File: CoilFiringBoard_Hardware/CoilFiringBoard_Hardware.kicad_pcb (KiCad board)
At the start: 2 copper layers, 96.5 x 71.1 mm, 19 parts, among them Q1 Q_NMOS_GDS, Q2 Q_NMOS_GDS, Q3 Q_NMOS_GDS, Q4 Q_NMOS_GDS

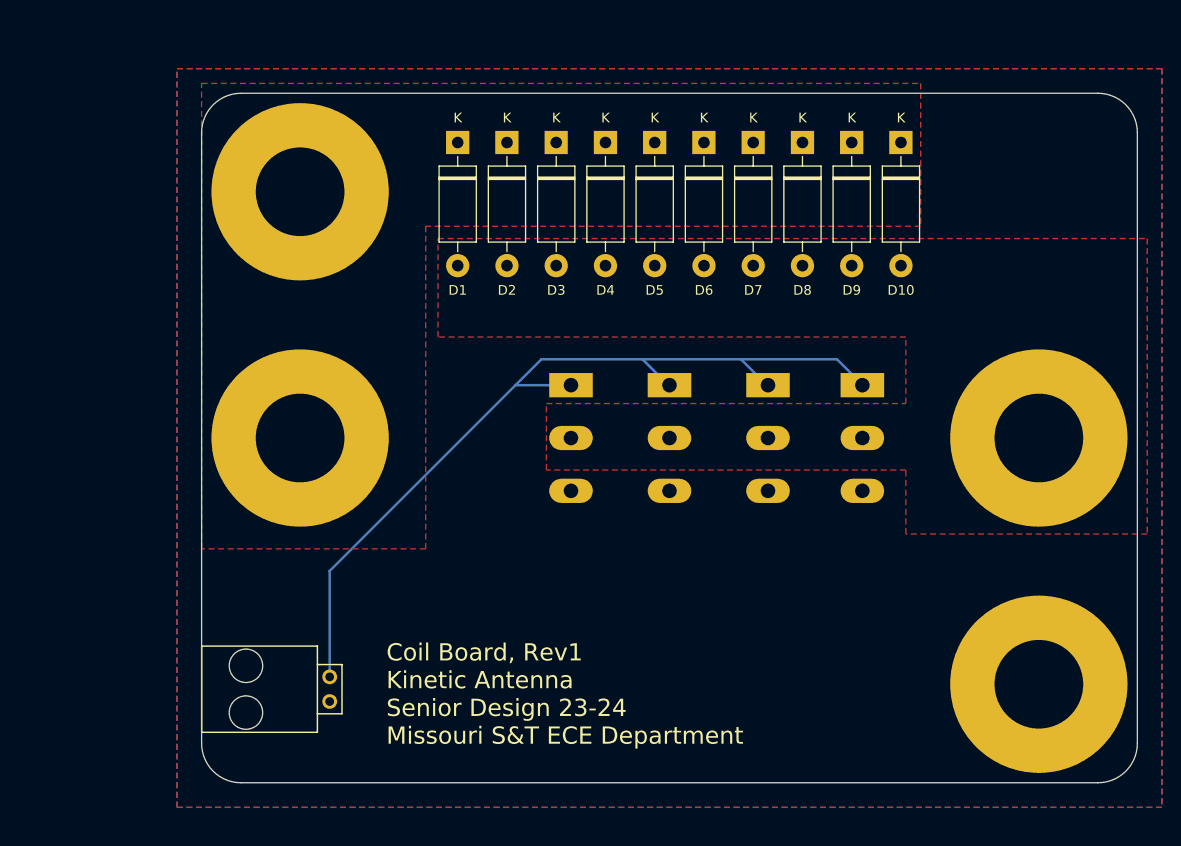
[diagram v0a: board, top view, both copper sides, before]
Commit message: Updated layout
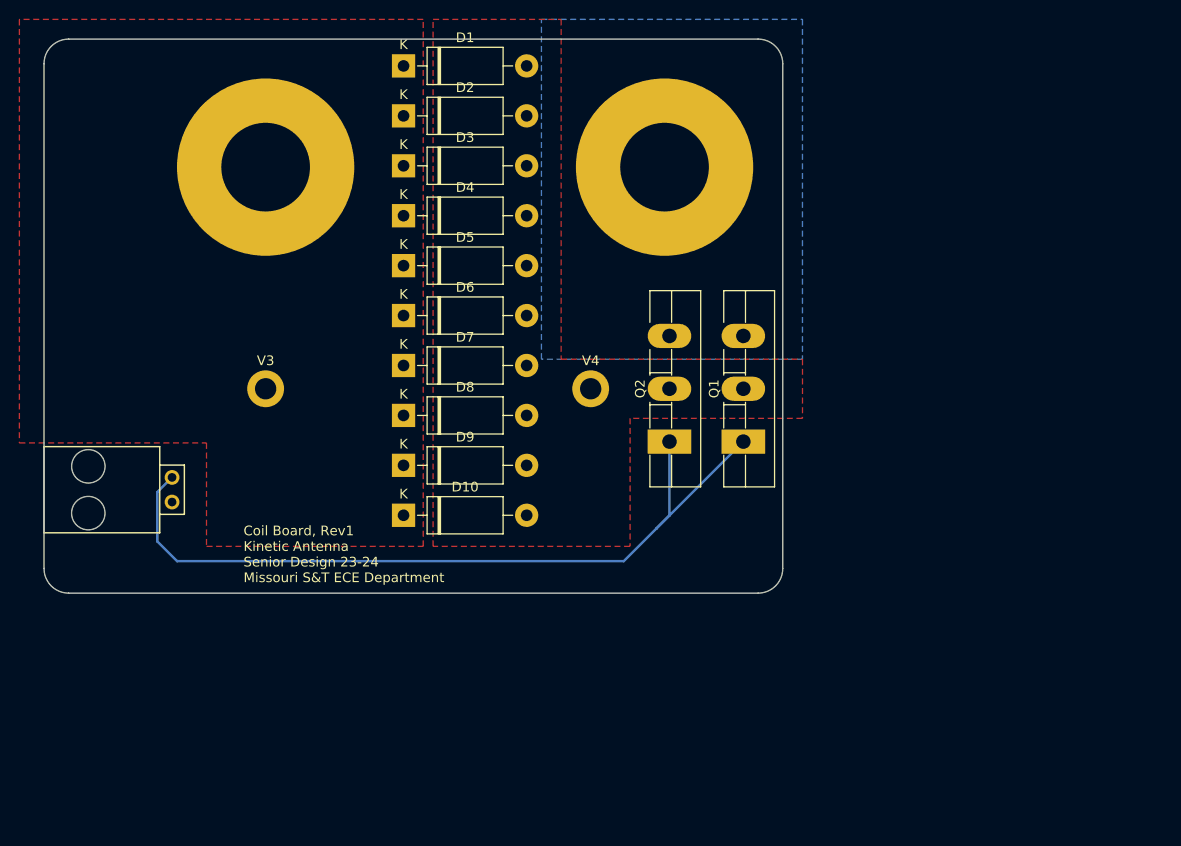
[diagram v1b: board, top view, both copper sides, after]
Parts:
- removed Q3, Q4: Q_NMOS_GDS, Package_TO_SOT_THT:TO-264-3_Vertical
- Q1, Q2: moved to F.Cu
- V3, V4: footprint MRDT_Drill_Holes:BATT_PWR_VIA -> MountingHole:MountingHole_2.2mm_M2_DIN965_Pad
- moved V2 65.8 mm to (126.5, 48.3)
- moved D10 64.1 mm to (99.6, 84.2), turned to 0 degrees
- moved D9 57.0 mm to (99.6, 79.0), turned to 0 degrees
- moved D8 49.9 mm to (99.6, 73.9), turned to 0 degrees
- moved V4 46.5 mm to (118.9, 71.1)
- moved D7 42.8 mm to (99.6, 68.7), turned to 0 degrees
- moved D6 35.8 mm to (99.6, 63.6), turned to 0 degrees
- moved D5 28.9 mm to (99.6, 58.4), turned to 0 degrees
- moved Conn1 26.2 mm to (75.7, 82.8)
- moved D4 22.2 mm to (99.6, 53.3), turned to 0 degrees
- moved D3 15.9 mm to (99.6, 48.1), turned to 0 degrees
- moved Q1 13.6 mm to (134.6, 76.6), turned to 90 degrees
- moved Q2 11.7 mm to (127.0, 76.6), turned to 90 degrees
- moved D2 11.0 mm to (99.6, 43.0), turned to 0 degrees
- moved D1 9.68 mm to (99.6, 37.8), turned to 0 degrees
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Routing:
- net Net-(Q1-G): track 89.6 -> 83.1 mm
- removed copper zone on F.Cu, net GND
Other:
- board size 96.5 x 71.1 mm -> 76.2 x 57.1 mm

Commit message: Updated layout
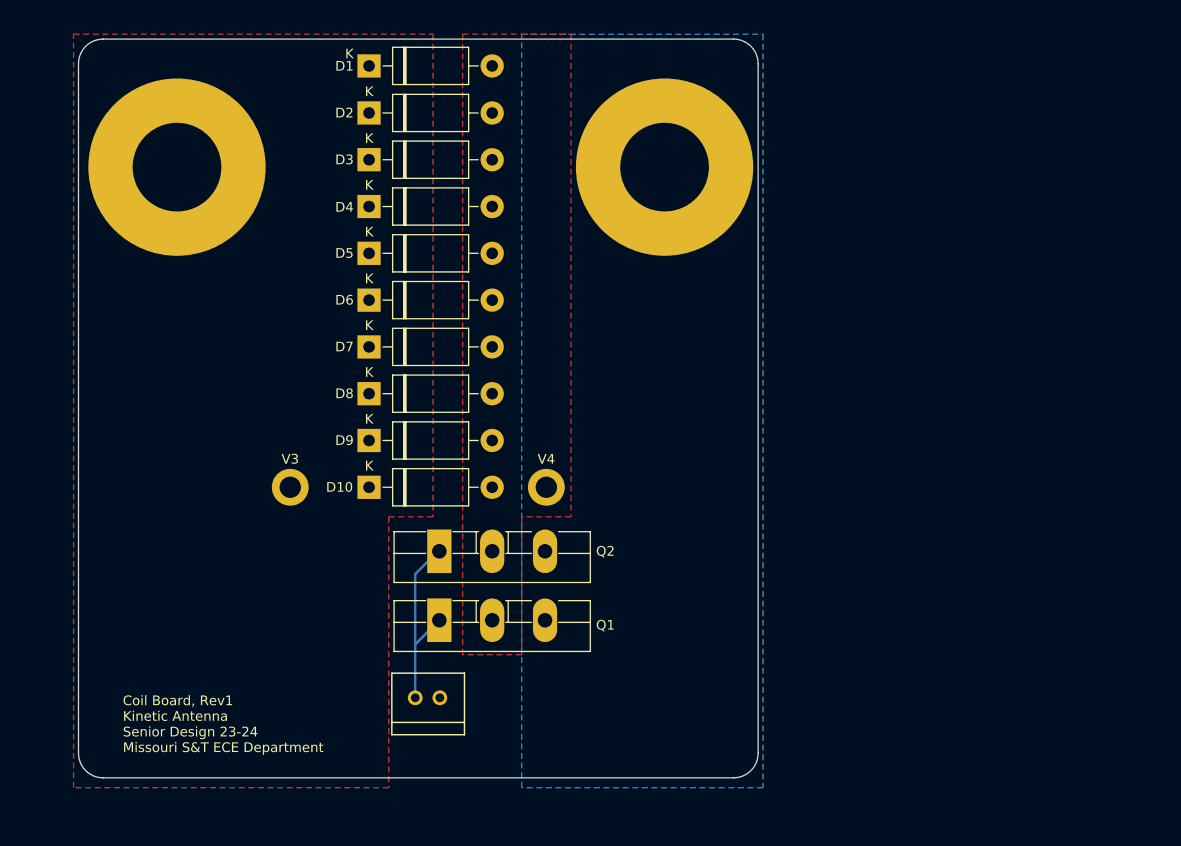
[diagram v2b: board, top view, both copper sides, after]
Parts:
- Conn1: footprint MRDT_Connectors:MOLEX_SL_02_Horizontal -> MRDT_Connectors:MOLEX_SL_02_Vertical
- moved Q1 36.4 mm to (103.3, 95.0), turned to 0 degrees
- moved Conn1 34.2 mm to (103.3, 103.0), turned to 180 degrees
- moved Q2 26.3 mm to (103.3, 87.9), turned to 0 degrees
- moved V4 11.1 mm to (114.3, 81.3)
- moved V3 10.5 mm to (87.9, 81.3)
- moved V1 9.14 mm to (76.2, 48.3)
- moved D10 4.58 mm to (96.0, 81.3)
- moved D9 4.39 mm to (96.0, 76.5)
- moved D8 4.20 mm to (96.0, 71.6)
- moved D7 4.04 mm to (96.0, 66.8)
- moved D6 3.90 mm to (96.0, 62.0)
- moved D5 3.78 mm to (96.0, 57.1)
- moved D4 3.68 mm to (96.0, 52.3)
- moved D3 3.61 mm to (96.0, 47.5)
- moved D2 3.57 mm to (96.0, 42.7)
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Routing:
- net Net-(Q1-G): track 83.1 -> 19.7 mm
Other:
- board size 76.2 x 57.1 mm -> 70.1 x 76.2 mm

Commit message: Increased spacing + added Y cap
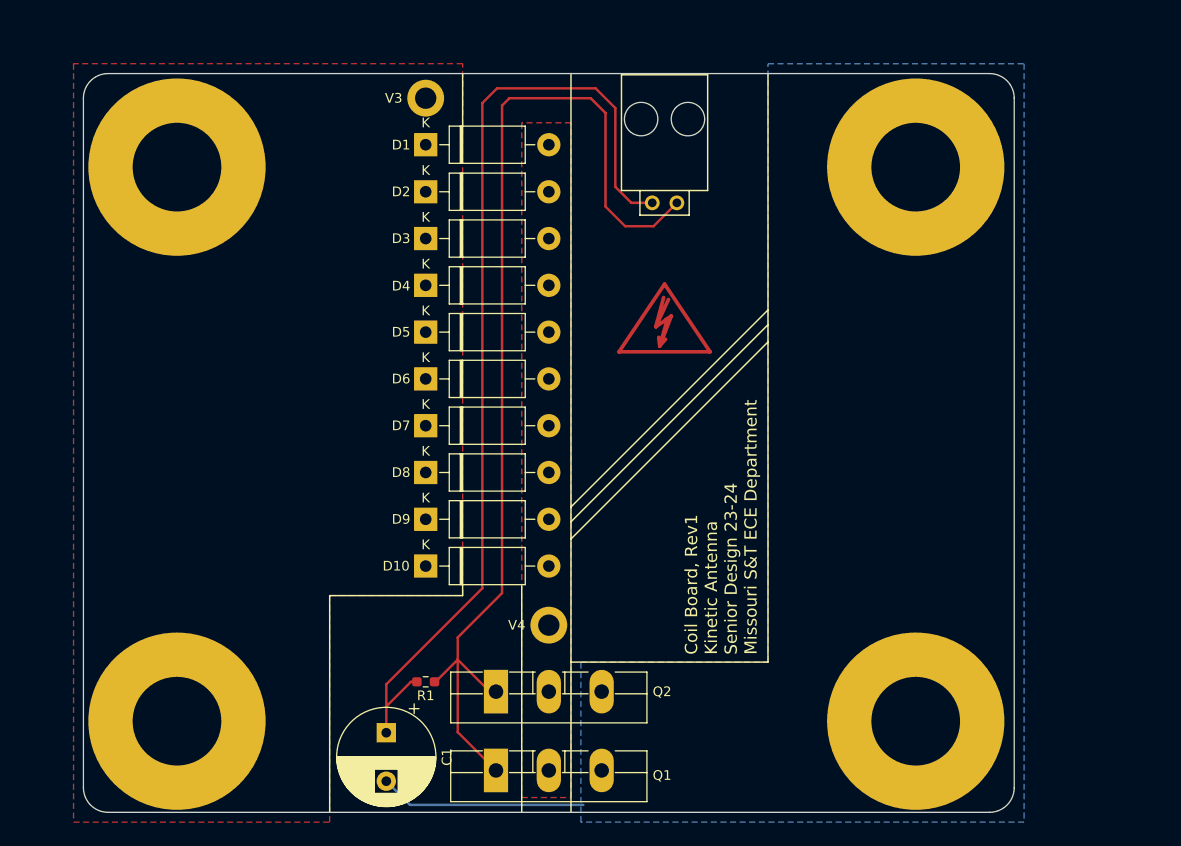
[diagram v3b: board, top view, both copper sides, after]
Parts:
- added C1: 4.7n, Capacitor_THT:CP_Radial_D10.0mm_P5.00mm, F.Cu at (97.8, 106.6)
- added R1: 4.7k, Resistor_SMD:R_0603_1608Metric_Pad0.98x0.95mm_HandSolder, F.Cu at (101.9, 101.3)
- added REF**: Symbol_HighVoltage_Type2_CopperTop_VerySmall, Symbol:Symbol_HighVoltage_Type2_CopperTop_VerySmall, F.Cu at (126.5, 64.5)
- added V5: Via, MRDT_Drill_Holes:BATT_PWR_VIA, F.Cu at (76.2, 105.4)
- added V6: Via, MRDT_Drill_Holes:BATT_PWR_VIA, F.Cu at (152.4, 105.4)
- Conn1: footprint MRDT_Connectors:MOLEX_SL_02_Vertical -> MRDT_Connectors:MOLEX_SL_02_Horizontal
- moved Conn1 55.6 mm to (125.2, 51.9), turned to 0 degrees
- moved V3 42.5 mm to (101.9, 41.1)
- moved V2 25.9 mm to (152.4, 48.3)
- moved Q1 16.6 mm to (109.1, 110.5)
- moved Q2 15.6 mm to (109.1, 102.4)
- moved V4 14.2 mm to (114.6, 95.5)
- moved D5 10.0 mm to (101.9, 65.3)
- moved D1 10.0 mm to (101.9, 45.9)
- moved D10 10.0 mm to (101.9, 89.4)
- moved D2 10.0 mm to (101.9, 50.8)
- moved D3 10.0 mm to (101.9, 55.6)
- moved D4 10.0 mm to (101.9, 60.5)
- moved D6 10.0 mm to (101.9, 70.1)
- moved D7 10.0 mm to (101.9, 74.9)
- moved D8 10.0 mm to (101.9, 79.8)
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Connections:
- Conn1 pad 1: unconnected-(Conn1-Pad1) -> GND1
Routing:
- net GND1: track 0.00 -> 101.1 mm
- net Net-(Q1-G): track 19.7 -> 111.2 mm
- net GND: track 0.00 -> 21.3 mm
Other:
- board size 70.1 x 76.2 mm -> 96 x 76.2 mm

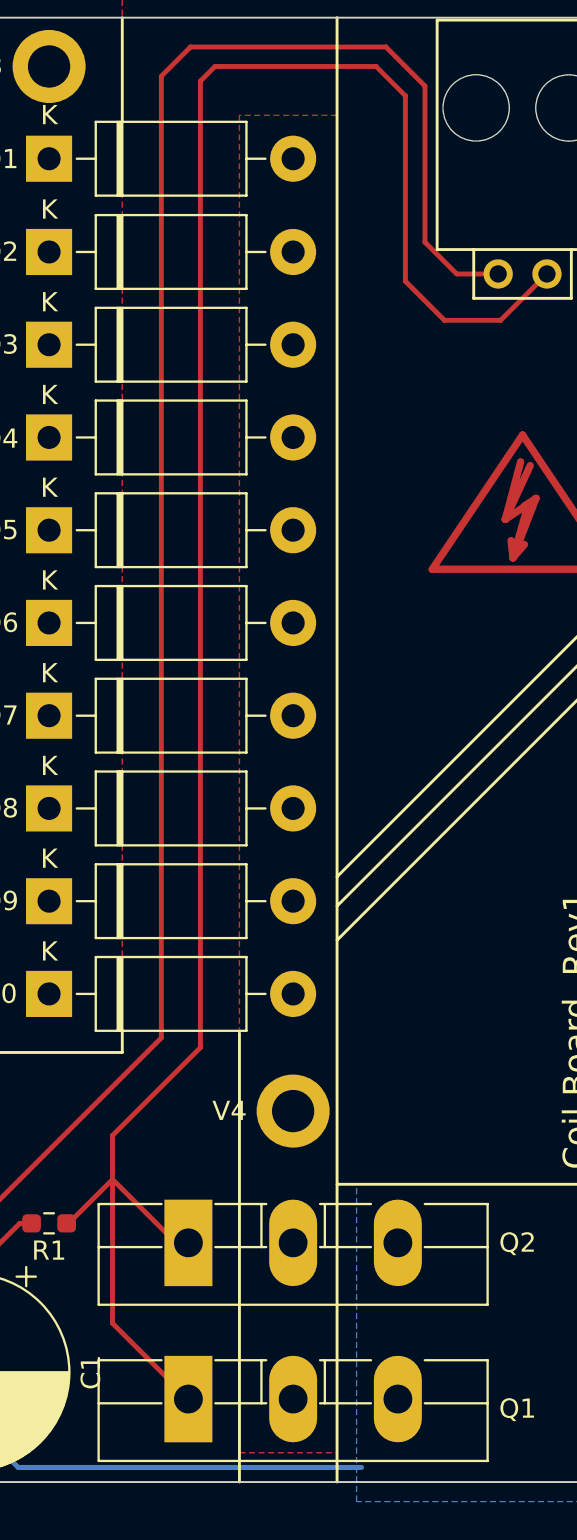
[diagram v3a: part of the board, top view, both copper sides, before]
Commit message: Updated Coil- plane
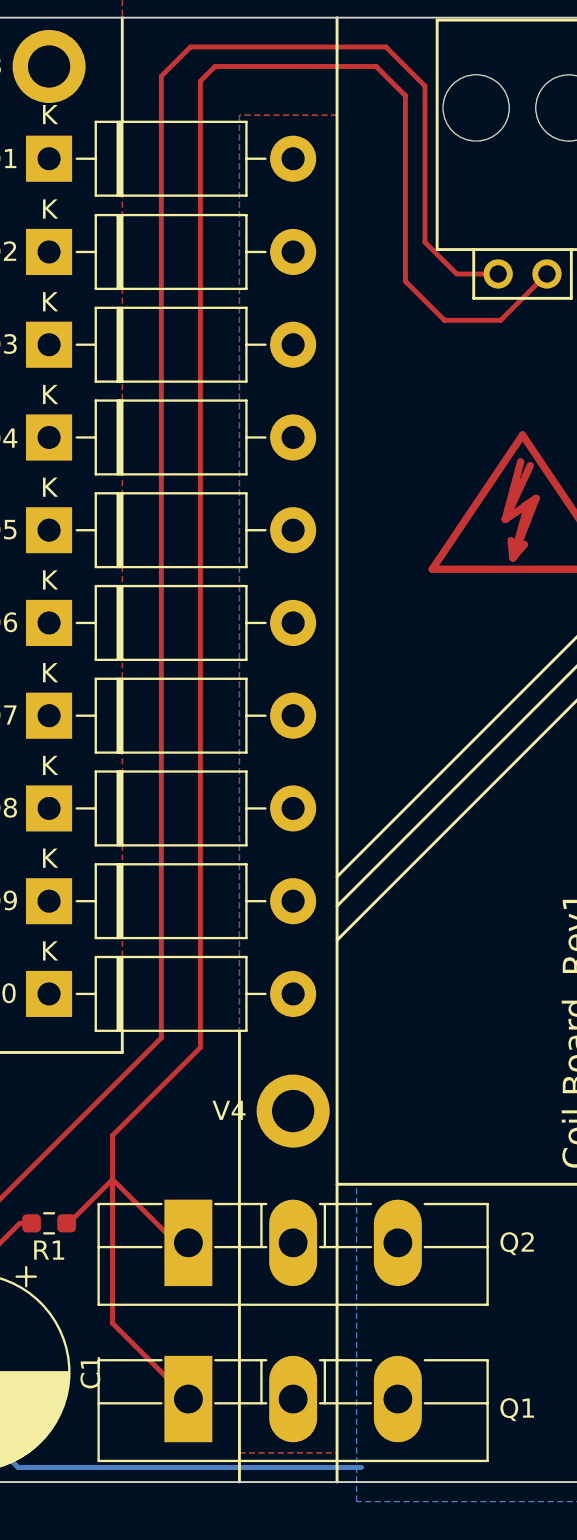
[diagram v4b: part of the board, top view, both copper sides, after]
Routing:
- added copper zone on B.Cu, net Coil-
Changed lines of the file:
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@@
   (segment (start 100.237677 114.046) (end 118.11 114.046) (width 0.254) (layer "B.Cu") (net 4))
   (segment (start 97.79 111.598323) (end 100.237677 114.046) (width 0.254) (layer "B.Cu") (net 4))
-  (zone (net 5) (net_name "Coil-") (layer "F.Cu") (hatch edge 0.5)
-    (priority 1)
-    (connect_pads yes (clearance 0.762))
-    (min_thickness 0.25) (filled_areas_thickness no)
-    (fill yes (thermal_gap 0.5) (thermal_bridge_width 0.5))
-    (polygon
-      (pts
-        (xy 111.76 113.284)
-        (xy 116.84 113.284)
-        (xy 116.84 43.688)
-        (xy 111.76 43.688)
-      )
-    )
-  )
   (zone (net 3) (net_name "PWR") (layer "F.Cu") (hatch edge 0.5)
     (connect_pads yes (clearance 0.762))
@@
       )
     )
+  )
+  (zone (net 5) (net_name "Coil-") (layers "F&B.Cu") (hatch edge 0.5)
+    (priority 1)
+    (connect_pads yes (clearance 0.762))
+    (min_thickness 0.25) (filled_areas_thickness no)
+    (fill yes (thermal_gap 0.5) (thermal_bridge_width 0.5))
+    (polygon
+      (pts
+        (xy 111.76 113.284)
+        (xy 116.84 113.284)
+        (xy 116.84 43.688)
+        (xy 111.76 43.688)
+      )
+    )

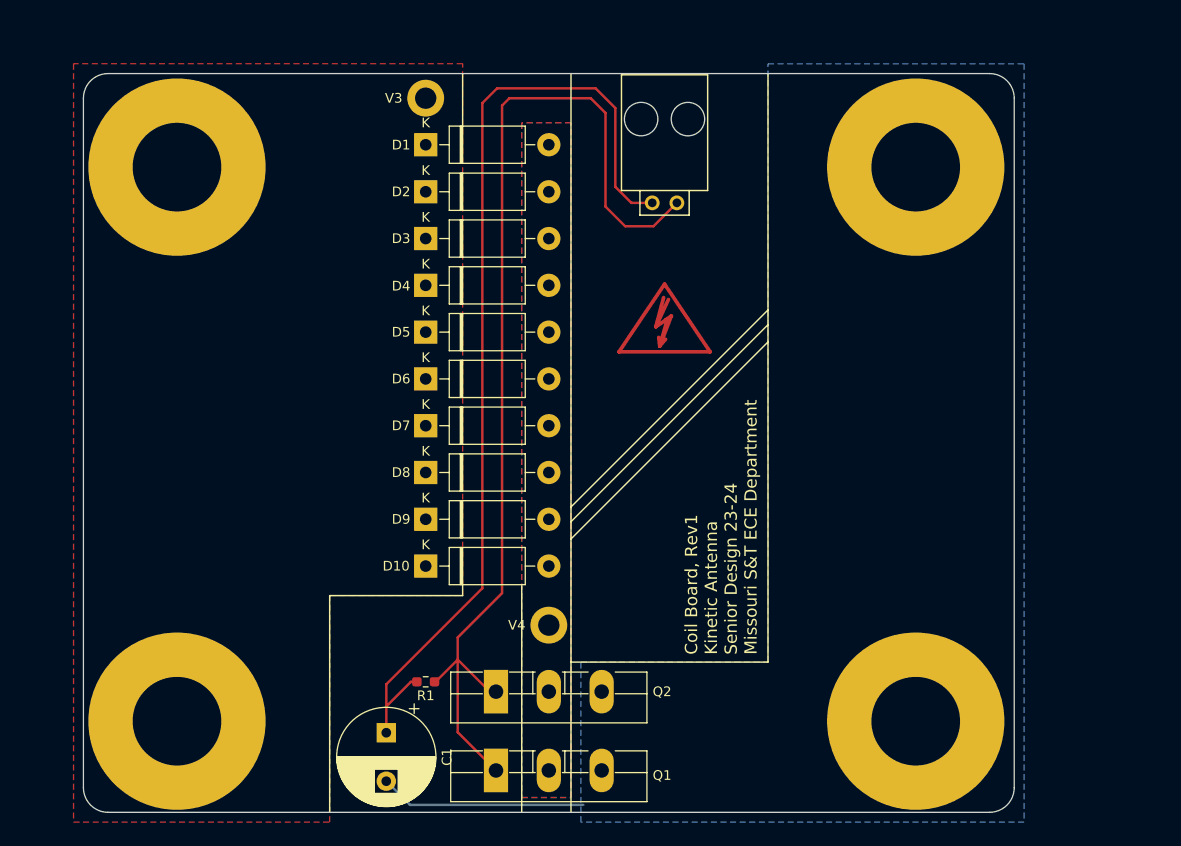
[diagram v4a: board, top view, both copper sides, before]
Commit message: Adjusted pads and traces
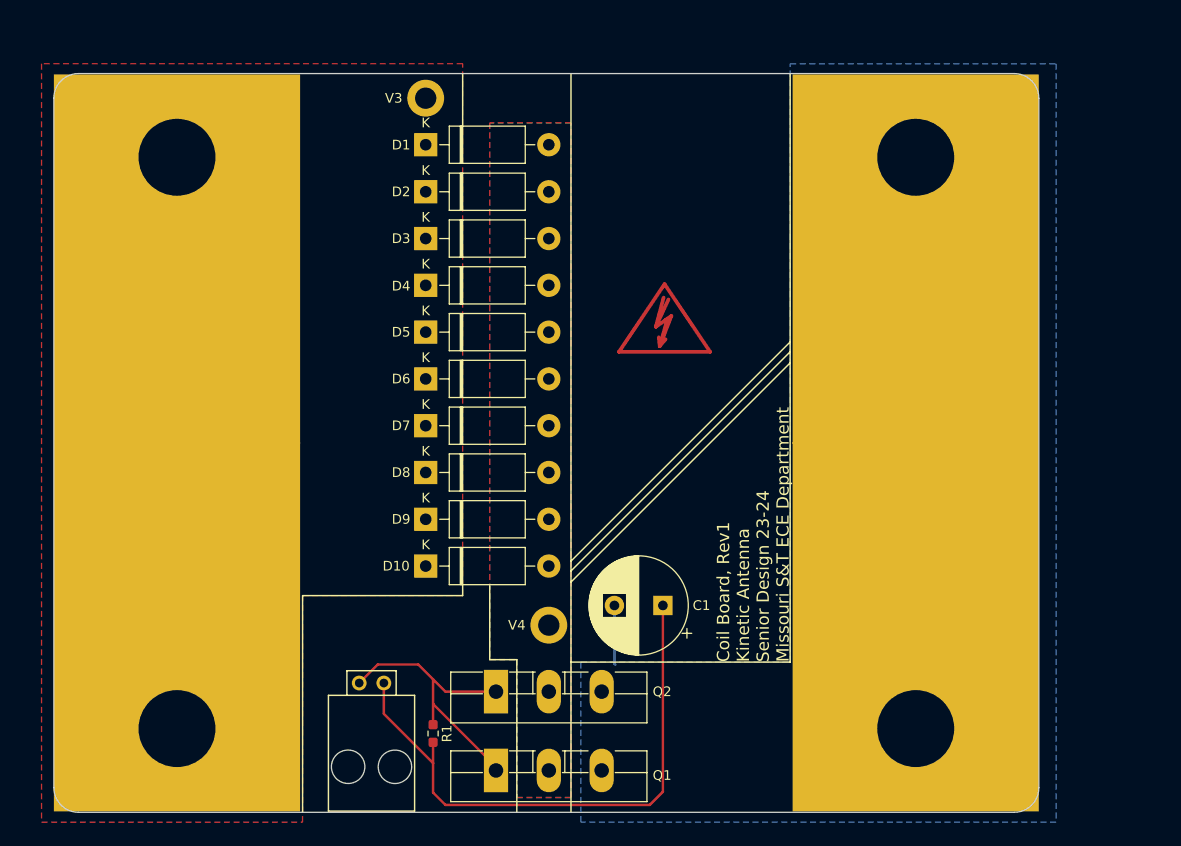
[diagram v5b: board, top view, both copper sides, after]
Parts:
- moved Conn1 56.7 mm to (97.5, 101.5), turned to 180 degrees
- moved C1 31.4 mm to (126.3, 93.5), turned to 180 degrees
- moved R1 5.39 mm to (102.6, 106.7), turned to -90 degrees
- moved V1 1.02 mm to (76.2, 47.2)
- moved V2 1.02 mm to (152.4, 47.2)
- moved V5 0.76 mm to (76.2, 106.2)
- moved V6 0.76 mm to (152.4, 106.2)
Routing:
- net Net-(Q1-G): track 111.2 -> 30.3 mm
- net GND1: track 101.1 -> 59.6 mm
- net GND: track 21.3 -> 6.13 mm
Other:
- board size 96 x 76.2 mm -> 101.6 x 76.2 mm
